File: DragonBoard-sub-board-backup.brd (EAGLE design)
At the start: 160 x 100 mm, 15 parts, among them U1 TXB0108PWR, U2 TXB0108PWR, U3 62674-301121ALF, U4 62674-301121ALF

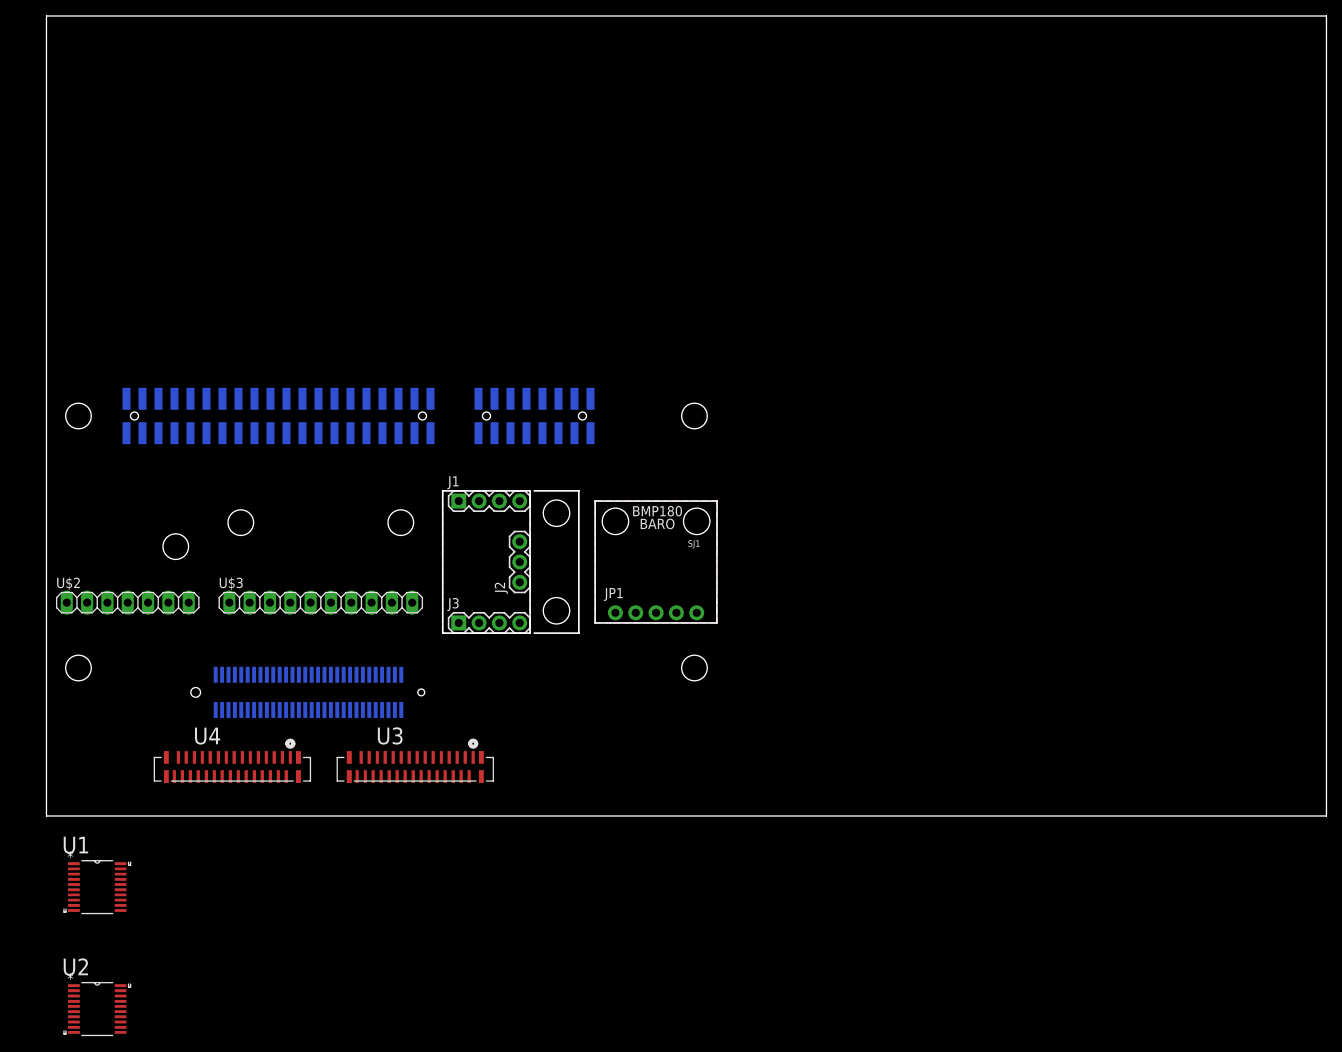
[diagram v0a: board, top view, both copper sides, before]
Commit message: added ftdi chip
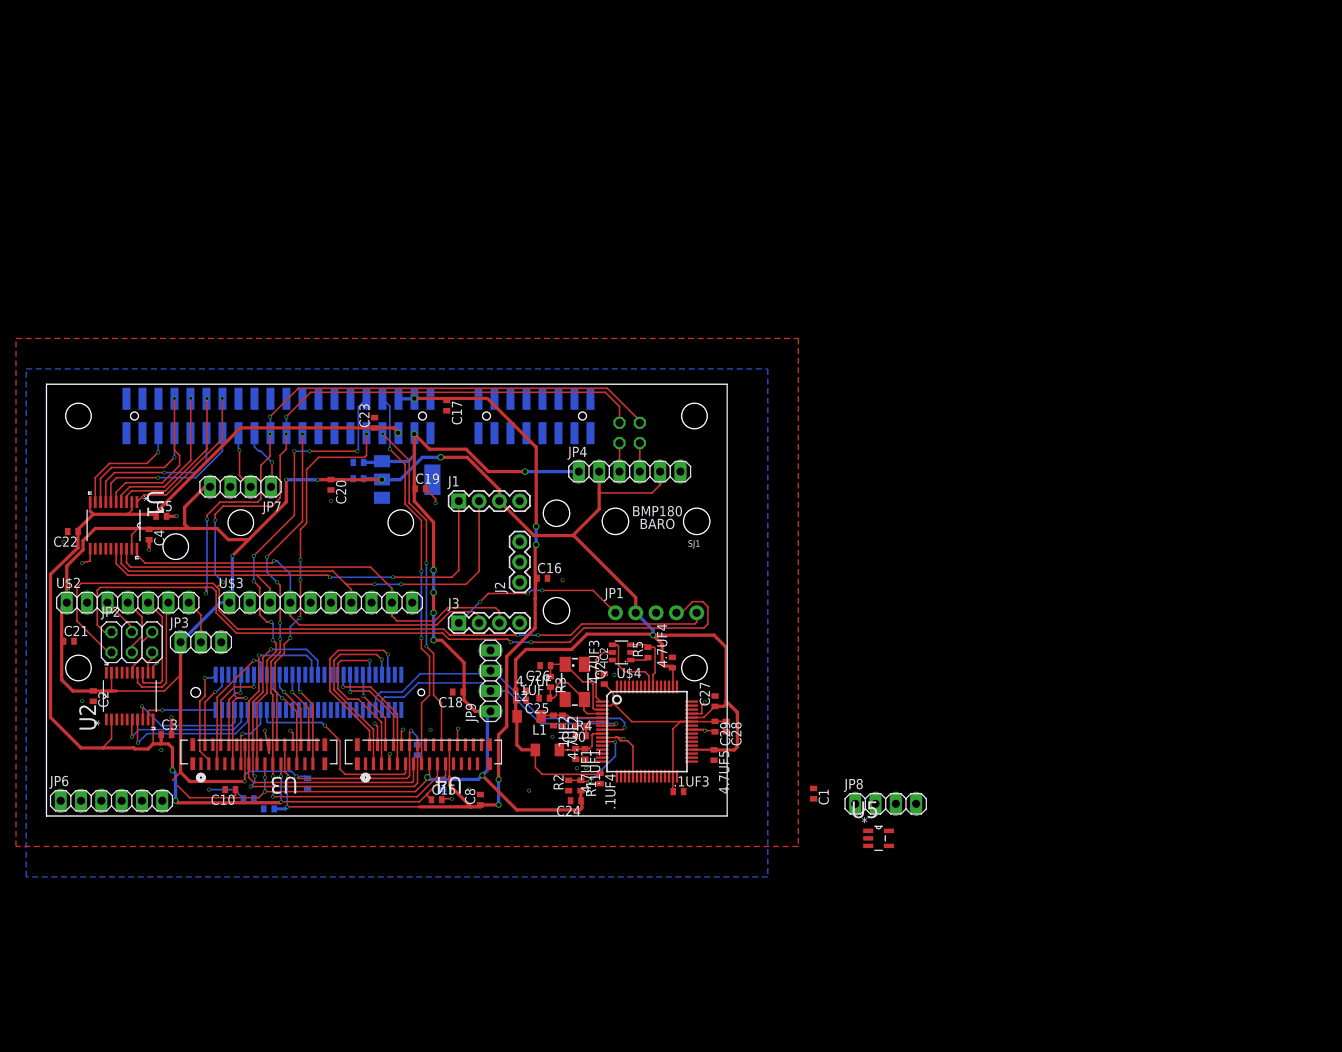
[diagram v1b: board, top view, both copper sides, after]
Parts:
- added .1UF, .1UF1, .1UF2, .1UF3, .1UF4, 4.7UF, 4.7UF1, 4.7UF2, 4.7UF3, 4.7UF4, 4.7UF5, C1, C10, C11, C12, C13, C14, C15, C16, C17, C18, C19, C2, C20, C21, C22, C23, C24, C25, C26, C27, C28, C29, C3, C30, C4, C5, C6, C7, C8, C9: (no value), rcl:C0402
- added IC1: REG1117, burr-brown:SOT223
- added IC2: 93AA76A, microchip:SOT23-6
- added JP2: (no value), pinhead:2X03
- added JP3: (no value), pinhead:1X03
- added JP4, JP6: (no value), pinhead:1X06
- added JP5: (no value), pinhead:2X02
- added JP7, JP8, JP9: (no value), pinhead:1X04
- added L1, L2: (no value), rcl:L3216C
- added Q2: 8MHz, crystal:CTS406
- added R1, R2, R3, R4, R5: (no value), rcl:R0402
- added U$4: FT423H, FT432H:LQFP-64
- added U5: NC7ST04M5X, pca9685:SOT95P280X145-5N
- moved U1 45.3 mm to (8.38, 36.3), turned to 270 degrees
- moved U2 39.3 mm to (10.4, 15.0), turned to 90 degrees
- moved U3 35.1 mm to (19.3, 11.3), turned to 180 degrees
- moved U4 12.8 mm to (39.9, 11.3), turned to 180 degrees
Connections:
- removed net !CS: J3.3
- removed net AD0/SDO: J3.2
- removed net FSYNC: J2.2
- removed net I2C_SDA: U$1.LS21
- removed net N$13: U1.12, U2.12
- removed net N$15: U1.14, U2.14
- removed net N$16: U1.15, U2.15
- removed net N$18: U1.17, U2.17
- removed net N$19: U1.18, U2.18
- removed net N$20: U1.20, U2.20
- removed net SCL: JP1.4
- removed net SCL/SCLK: J1.1
- removed net SDA: JP1.5
- removed net SDA/SDI: J1.2
- removed net SPI1_CS_N: U2.8
- removed net VDD: J1.3, JP1.2
- new net 3.3V: IC2.6
- new net CAM_SCL: U$1.HS32, U3.13, U4.13
- new net CAM_SDA: U$1.HS34, U3.14, U4.14
- new net CON_RX: JP6.4, U1.15
- new net CON_TX: JP6.5, U1.14
- new net CSI0_C+: U$1.HS2, U3.3
- new net CSI0_C-: U$1.HS4, U3.2
- new net CSI0_D0+: U$1.HS8, U3.9
- new net CSI0_D0-: U$1.HS10, U3.8
- new net CSI0_D1+: U$1.HS14, U3.6
- new net CSI0_D1-: U$1.HS16, U3.5
- new net CSI0_D2+: U$1.HS20, U3.25
- new net CSI0_D2-: U$1.HS22, U3.26
- new net CSI0_D3+: U$1.HS26, U3.28
- new net CSI0_D3-: U$1.HS28, U3.29
- new net CSI1_C+: U$1.HS54, U4.3
- new net CSI1_C-: U$1.HS56, U4.2
- new net CSI1_D0+: U$1.HS42, U4.9
- new net CSI1_D0-: U$1.HS44, U4.8
- new net CSI1_D1+: U$1.HS48, U4.6
- new net CSI1_D1-: U$1.HS50, U4.5
- new net DSI_CLK+: U$1.HS21
- new net DSI_CLK-: U$1.HS23
- new net DSI_D0+: U$1.HS27
- new net DSI_D0-: U$1.HS29
- new net DSI_D1+: U$1.HS33
- new net DSI_D1-: U$1.HS35
- new net DSI_D2+: U$1.HS39
- new net DSI_D2-: U$1.HS41
- new net DSI_D3+: U$1.HS45
- new net DSI_D3-: U$1.HS47
- new net EECLK: IC2.4, U$4.56
- new net EECS: IC2.5, U$4.1
- new net EEDATA: IC2.3, R5.2, U$4.55
- new net GPS_RX: U1.13
- new net GPS_TX: U1.12
- new net HSIC_DATA: U$1.HS59
- new net HSIC_STR: U$1.HS57
- new net I2C1_SDA: JP1.5, JP2.1, JP5.4, U$1.LS21
- new net I2C3_SCL: U$1.HS36
- new net I2C3_SDA: U$1.HS38
- new net MCLK0: U$1.HS15, U3.11
- new net MCLK1: U$1.HS17, U4.11
- new net N$1: JP3.2, U$2.7
- new net N$10: U$3.6
- new net N$11: C25.1, Q2.3, R3.2, U$4.4
- new net N$12: U$3.8
- new net N$2: JP2.3, U$2.4
- new net N$3: JP2.4, U$2.3
- new net N$4: JP4.4, JP5.1
- new net N$5: JP4.3, JP5.3
- new net N$6: C30.1, R4.2, U$4.6
- new net N$7: C26.1, Q2.1, R3.1, U$4.3
- new net N$8: U$3.5
- new net SBUS: JP8.2, U5.2
- new net SPI1_CS: U$1.HS7, U2.8
- new net SPI_A_CLK: J1.1, U$3.3, U1.16
- new net SPI_A_CS: J3.3, U$3.9, U1.18
- new net SPI_A_MISO: J1.2, U$3.7, U1.17
- new net SPI_A_MOSI: J3.2, U$3.4, U1.20
- new net SPI_B_CLK: JP2.6, U2.15
- new net SPI_B_CS: U$2.5, U2.13
- new net SPI_B_MISO: U$2.6, U2.14
- new net SPI_B_MOSI: JP2.5, U2.12
- new net USB_D+: JP9.3, U$1.HS51, U$4.8
- new net USB_D-: JP9.2, U$1.HS53, U$4.7
- new net VCORE: .1UF3.1, 4.7UF3.1, C28.1, C29.1, U$4.2, U$4.31, U$4.43
- new net VPHY: .1UF2.1, 4.7UF2.1, L2.2, U$4.5
- new net VPLL: .1UF1.1, 4.7UF1.1, L1.2, U$4.9
- new net _SBUS: JP8.1, U5.4
- net +1.8V: now also C14.1, C15.1, C22.1, C23.1, C3.1, C5.1, U3.21, U4.21
- net +3.3V: now also .1UF.1, .1UF4.1, 4.7UF.1, 4.7UF4.1, 4.7UF5.1, C1.1, C12.1, C13.1, C2.1, C20.1, C21.1, C27.1, C4.1, C7.1, IC1.2, J1.3, JP1.2, JP3.1, JP4.2, JP4.5, JP7.4, L1.1, L2.1, U$2.1, U$3.1, U$4.16, U$4.36, U$4.44, U$4.50, U3.12, U4.12, U5.5
- net +5V: now also C10.1, C11.1, C18.1, C19.1, C24.1, C6.1, IC1.3, JP4.1, JP8.3, JP9.1, R1.2, U3.17, U4.17
- net FLASH: now also U3.19, U4.19
- net GND: now also .1UF.2, .1UF1.2, .1UF2.2, .1UF3.2, .1UF4.2, 4.7UF.2, 4.7UF1.2, 4.7UF2.2, 4.7UF3.2, 4.7UF4.2, 4.7UF5.2, C1.2, C10.2, C11.2, C12.2, C13.2, C14.2, C15.2, C16.2, C17.2, C18.2, C19.2, C2.2, C20.2, C21.2, C22.2, C23.2, C24.2, C25.2, C26.2, C27.2, C28.2, C29.2, C3.2, C30.2, C4.2, C5.2, C6.2, C7.2, C8.2, C9.2, IC1.1, IC2.2, J2.2, JP3.3, JP4.6, JP6.1, JP7.3, JP8.4, JP9.4, R2.1, R4.1, U$2.2, U$3.10, U$3.2, U$4.10, U$4.21, U$4.41, U$4.45, U2.11, U3.1, U3.10, U3.16, U3.18, U3.23, U3.24, U3.27, U3.30, U3.4, U3.7, U4.1, U4.10, U4.16, U4.18, U4.23, U4.24, U4.27, U4.30, U4.4, U4.7, U5.3
- net I2C0_SCL: now also JP7.2
- net I2C0_SDA: now also JP7.1
- net I2C1_SCL: now also JP1.4, JP2.2, JP5.2
- net N$14: now also IC2.1, R5.1; no longer U1.13, U2.13
- net N$17: now also R1.1, R2.2, U$4.11; no longer U1.16, U2.16
- net RESET0: now also U3.20
- net RESET1: now also U4.20
- net SPI0_CLK: now also U1.5; no longer U1.6
- net SPI0_CS_N: now also U1.3; no longer U1.8
- net SPI0_MISO: now also U1.4; no longer U1.7
- net SPI0_MOSI: now also U1.1; no longer U1.9
- net SPI1_CLK: now also U$1.HS9
- net SPI1_MISO: now also U$1.HS11
- net SPI1_MOSI: now also U$1.HS1
- net STANDBY0: now also U3.15
- net STANDBY1: now also U4.15
- net SYS_DCIN: now also C16.1, C17.1, C8.1, C9.1, U3.22, U4.22
- net UART0_RX: now also U1.8; no longer U1.1
- net UART0_TX: now also U1.9; no longer U1.3
- net UART1_RX: now also U1.6; no longer U1.5
- net UART1_TX: now also U1.7; no longer U1.4
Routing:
- net +3.3V: track 0.00 -> 327.2 mm, vias 0 -> 9
- net I2C1_SCL: track 0.00 -> 174.0 mm, vias 0 -> 6
- net I2C1_SDA: track 0.00 -> 169.0 mm, vias 0 -> 6
- net +1.8V: track 0.00 -> 153.3 mm, vias 0 -> 5
- net +5V: track 0.00 -> 146.2 mm, vias 0 -> 10
- net SYS_DCIN: track 0.00 -> 114.6 mm, vias 0 -> 7
- net FLASH: track 0.00 -> 71.7 mm, vias 0 -> 7
- net SPI_A_MISO: track 0.00 -> 59.7 mm, vias 0 -> 2
- net STANDBY0: track 0.00 -> 58.5 mm, vias 0 -> 7
- net SPI_A_CLK: track 0.00 -> 58.5 mm, vias 0 -> 2
- net SPI_A_CS: track 0.00 -> 55.7 mm
- net CAM_SDA: track 0.00 -> 52.5 mm, vias 0 -> 3
- net SPI_A_MOSI: track 0.00 -> 52.1 mm, vias 0 -> 1
- net GND: track 0.00 -> 49.1 mm, vias 0 -> 29
- net STANDBY1: track 0.00 -> 48.5 mm, vias 0 -> 3
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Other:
- board size 160 x 100 mm -> 85.1 x 54 mm
